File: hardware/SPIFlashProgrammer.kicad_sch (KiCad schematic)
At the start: 0 parts

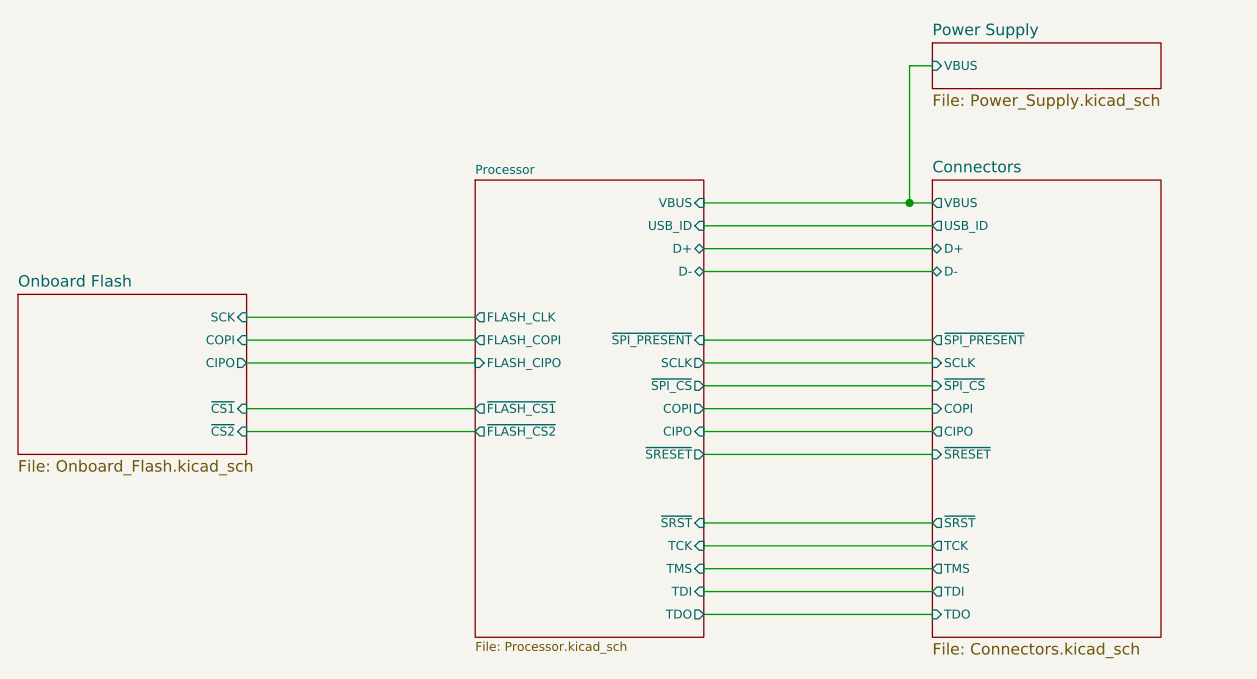
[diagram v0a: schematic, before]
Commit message: Added control for the level shifter output enable to the CPU to fix problems caused by us accidentally still driving the external bus after reset is released
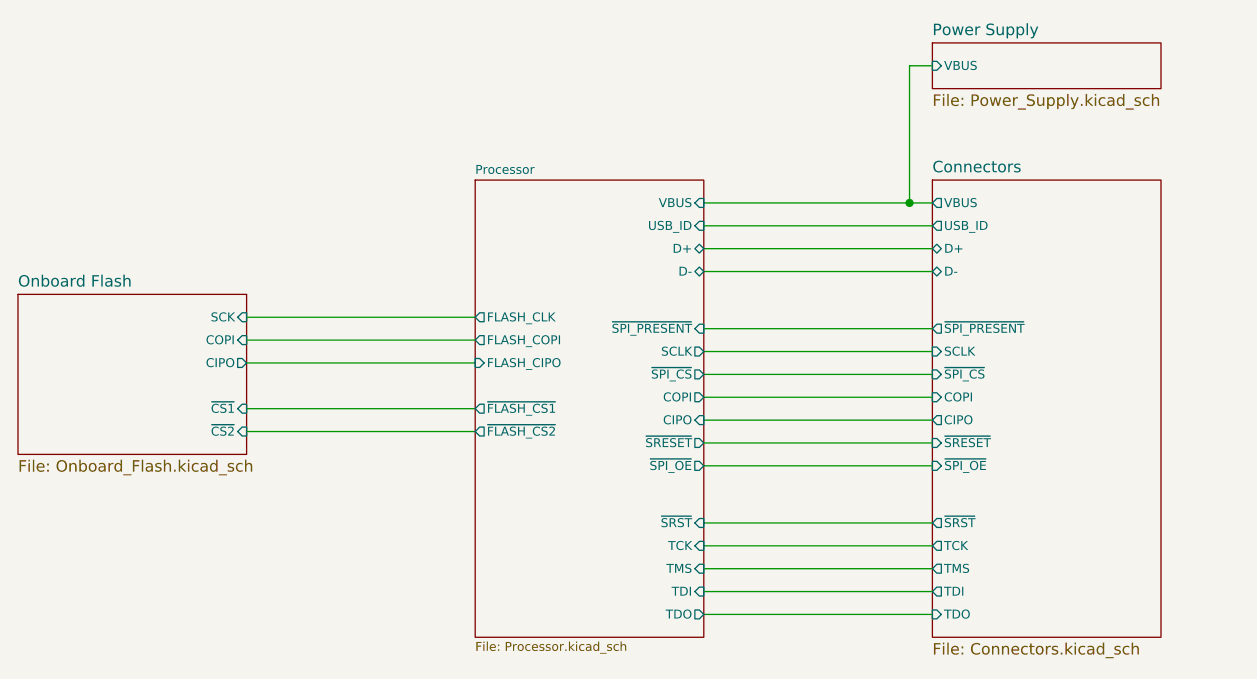
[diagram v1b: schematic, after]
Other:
- sheet Connectors ports: added ~{SPI_OE}; removed none
- sheet Processor ports: added ~{SPI_OE}; removed none
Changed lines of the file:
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@@
     (stroke (width 0) (type default) (color 0 0 0 0))
   )
-  (wire (pts (xy 177.8 110.49) (xy 152.4 110.49))
+  (wire (pts (xy 177.8 109.22) (xy 152.4 109.22))
     (stroke (width 0) (type default) (color 0 0 0 0))
   )
-  (wire (pts (xy 152.4 107.95) (xy 177.8 107.95))
+  (wire (pts (xy 152.4 106.68) (xy 177.8 106.68))
     (stroke (width 0) (type default) (color 0 0 0 0))
   )
@@
     (stroke (width 0) (type default) (color 0 0 0 0))
   )
-  (wire (pts (xy 152.4 113.03) (xy 177.8 113.03))
+  (wire (pts (xy 152.4 111.76) (xy 177.8 111.76))
     (stroke (width 0) (type default) (color 0 0 0 0))
   )
-  (wire (pts (xy 152.4 100.33) (xy 177.8 100.33))
+  (wire (pts (xy 152.4 99.06) (xy 177.8 99.06))
     (stroke (width 0) (type default) (color 0 0 0 0))
   )
-  (wire (pts (xy 152.4 102.87) (xy 177.8 102.87))
+  (wire (pts (xy 152.4 101.6) (xy 177.8 101.6))
     (stroke (width 0) (type default) (color 0 0 0 0))
   )
@@
     (stroke (width 0) (type default) (color 0 0 0 0))
   )
+  (wire (pts (xy 152.4 114.3) (xy 177.8 114.3))
+    (stroke (width 0) (type default) (color 0 0 0 0))
+  )
   (wire (pts (xy 101.6 110.49) (xy 127 110.49))
     (stroke (width 0) (type default) (color 0 0 0 0))
@@
     (stroke (width 0) (type default) (color 0 0 0 0))
   )
-  (wire (pts (xy 177.8 105.41) (xy 152.4 105.41))
+  (wire (pts (xy 177.8 104.14) (xy 152.4 104.14))
     (stroke (width 0) (type default) (color 0 0 0 0))
   )
@@
       (effects (font (size 0.9906 0.9906)) (justify left top))
     )
-    (pin "SCLK" output (at 152.4 102.87 0)
+    (pin "SCLK" output (at 152.4 101.6 0)
       (effects (font (size 0.9906 0.9906)) (justify right))
     )
-    (pin "~{SPI_CS}" output (at 152.4 105.41 0)
+    (pin "~{SPI_CS}" output (at 152.4 104.14 0)
       (effects (font (size 0.9906 0.9906)) (justify right))
     )
-    (pin "COPI" output (at 152.4 107.95 0)
+    (pin "COPI" output (at 152.4 106.68 0)
       (effects (font (size 0.9906 0.9906)) (justify right))
     )
-    (pin "CIPO" input (at 152.4 110.49 0)
+    (pin "CIPO" input (at 152.4 109.22 0)
       (effects (font (size 0.9906 0.9906)) (justify right))
     )
-    (pin "~{SRESET}" output (at 152.4 113.03 0)
+    (pin "~{SRESET}" output (at 152.4 111.76 0)
       (effects (font (size 0.9906 0.9906)) (justify right))
     )
@@
       (effects (font (size 0.9906 0.9906)) (justify left))
     )
-    (pin "~{SPI_PRESENT}" input (at 152.4 100.33 0)
+    (pin "~{SPI_PRESENT}" input (at 152.4 99.06 0)
       (effects (font (size 0.9906 0.9906)) (justify right))
+    )
+    (pin "~{SPI_OE}" output (at 152.4 114.3 0)
+      (effects (font (size 1 1)) (justify right))
     )
   )
@@
       (effects (font (size 0.9906 0.9906)) (justify left))
     )
-    (pin "CIPO" output (at 177.8 110.49 180)
+    (pin "CIPO" output (at 177.8 109.22 180)
       (effects (font (size 0.9906 0.9906)) (justify left))
     )
-    (pin "SCLK" input (at 177.8 102.87 180)
+    (pin "SCLK" input (at 177.8 101.6 180)
       (effects (font (size 0.9906 0.9906)) (justify left))
     )
-    (pin "~{SPI_CS}" input (at 177.8 105.41 180)
+    (pin "~{SPI_CS}" input (at 177.8 104.14 180)
       (effects (font (size 0.9906 0.9906)) (justify left))
     )
-    (pin "~{SRESET}" input (at 177.8 113.03 180)
+    (pin "~{SRESET}" input (at 177.8 111.76 180)
       (effects (font (size 0.9906 0.9906)) (justify left))
     )
-    (pin "COPI" input (at 177.8 107.95 180)
+    (pin "COPI" input (at 177.8 106.68 180)
       (effects (font (size 0.9906 0.9906)) (justify left))
     )
@@
       (effects (font (size 0.9906 0.9906)) (justify left))
     )
-    (pin "~{SPI_PRESENT}" output (at 177.8 100.33 180)
+    (pin "~{SPI_PRESENT}" output (at 177.8 99.06 180)
       (effects (font (size 0.9906 0.9906)) (justify left))
     )
+    (pin "~{SPI_OE}" input (at 177.8 114.3 180)
+      (effects (font (size 1 1)) (justify left))
+    )
   )
